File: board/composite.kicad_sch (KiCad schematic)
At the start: 23 parts, among them J10 VGA, J6 COMPOSITE, U17 OBVID, Y1 14.318MHz, Y3 25.175MHz

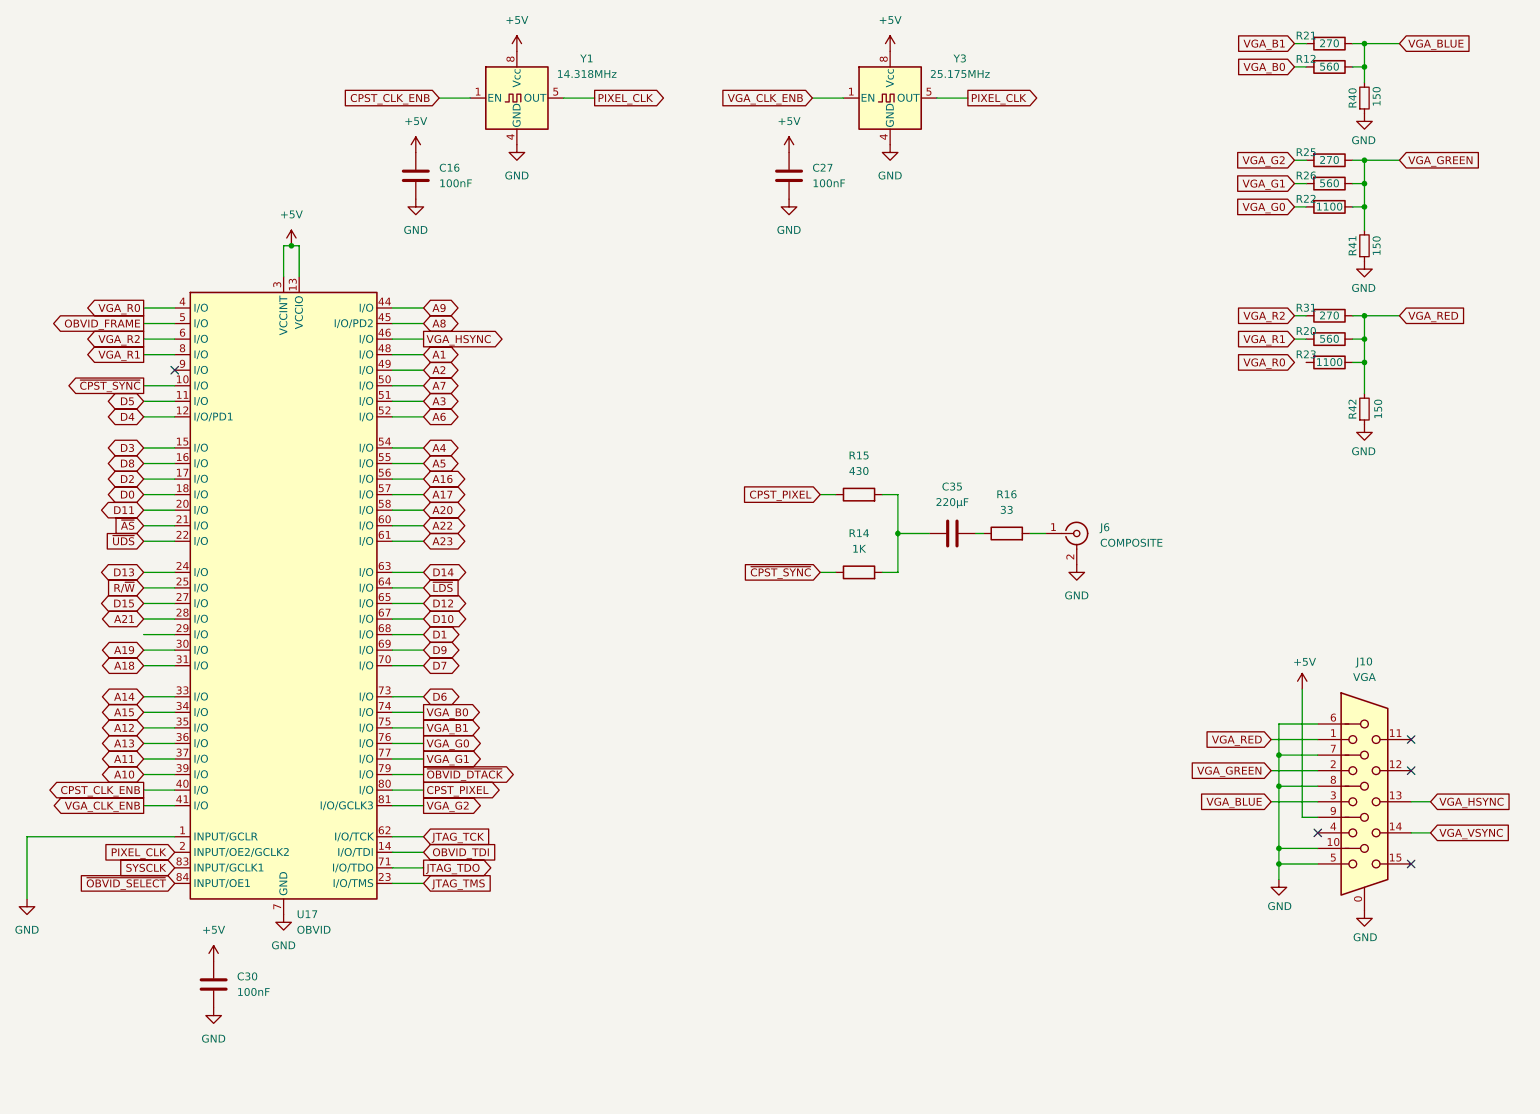
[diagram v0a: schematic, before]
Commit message: CF card, composite, VGA
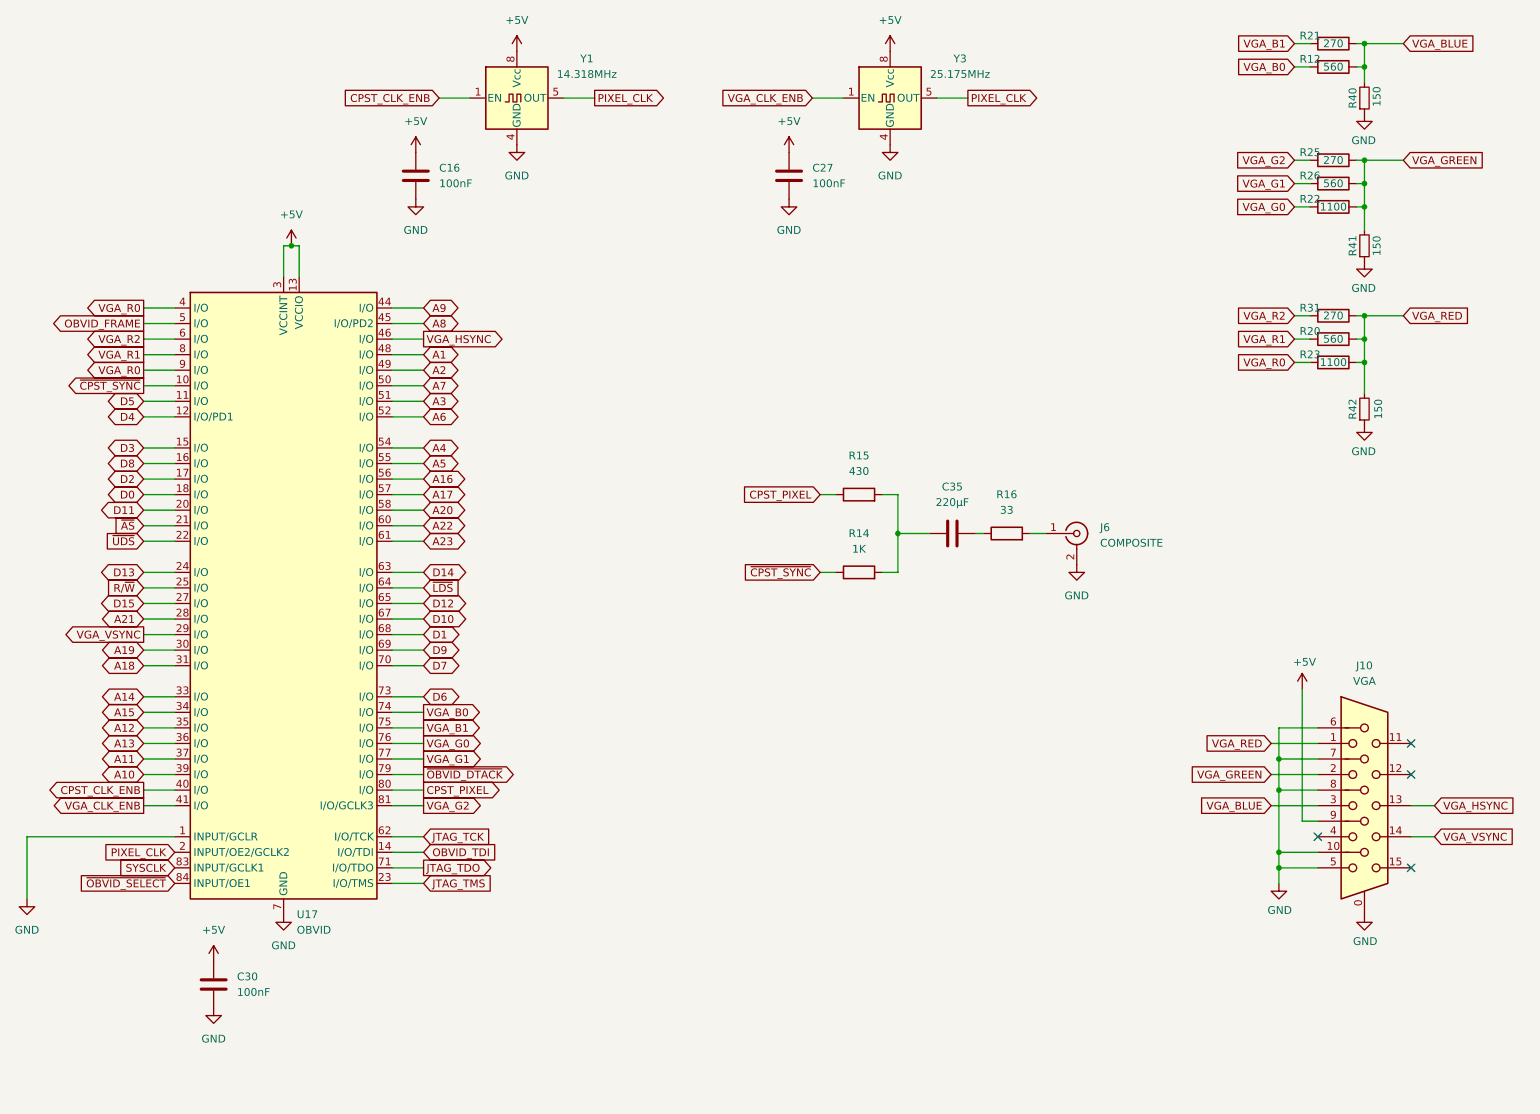
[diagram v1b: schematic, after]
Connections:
- net VGA_R0: now also R23.2, U17.9 (I/O)
- net VGA_VSYNC: now also U17.29 (I/O)
- no-connect marks 5 -> 4
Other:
- moved on the sheet: J10, R12, R20, R21, R22, R23, R25, R26, R31

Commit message: checkpoint
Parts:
- R22, R23: footprint Resistor_SMD:R_0603_1608Metric -> Resistor_THT:R_Axial_DIN0207_L6.3mm_D2.5mm_P10.16mm_Horizontal
- Y3: Digikey https://www.digikey.com/en/products/detail/shenzhen-sctf-electronics/SXOA14-31818A20F30TNN/25795979 -> https://www.digikey.com/en/products/detail/shenzhen-sctf-electronics/SXOA25-175A20F30TNN/25795923?s=N4IgjCBcpgbFoDGUBmBDANgZwKYBoQB7KAbRACYBOAFgAZZKQBdAgBwBcoQBldgJwCWAOwDmIAL4Fq8aCGSR02fEVIUArAHZ6zNp0g9%2BwsZJAMEc1JlwFikMtTBgAHJQ06QHLr0GiJBDRCy8orWKnYgAMwRYGpObiweegY%2BxgSOtObBVsq2ZBHU1OS0GQme%2Bt5GfuBOEZmWSjaqheQalIylSRW%2BJuRq5HUK2Y3h5GDksGDxul6G3QS9tUH1obkUE9TuZcmVPRoySMs5quTUlJMQHTMpVVpuS4MNYWQX0%2BWzqeCOgQcPK6oviSuOzSY2%2BFl%2BR3CMTiERKr22c3AETUG3uIUhz02nXeVRixQG6OGz1OtH6lze1xMYEoLgJQyeIBKPVolH6aPpqwBWy6H1Gagy7Meq16ADpJmoAAQAWQAEgAvLFcACqQgE7AA8igpTg0FgAK58HBVchRJx0oWqKL8yhwwEU4EgAC0YKyFvCsT6zBMjtRP0JDNgESoZO9anNfyh8XE0aAA
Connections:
- net A12 renamed ~{FC2}
- net A14 renamed ~{FC0}
- net A15 renamed ~{FC1}
- net OBVID_FRAME renamed ~{OBVID_IRQ}
- net SYSCLK renamed CPUCLK
- net ~{OBVID_DTACK} renamed OBVID_STALL
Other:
- moved on the sheet: C30, U17

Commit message: Board rev1 PCB complete, already have a spot fix
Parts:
- added J5: JTAG BYPASS, Connector_PinHeader_2.54mm:PinHeader_1x02_P2.54mm_Vertical, symbol Connector:Conn_01x02_Pin
- J10: footprint board:HD15-SN-24 -> board:AMPHENOL_ICD15S13E4GX00LF; symbol Connector:DE15_Socket_HighDensity_MountingHoles -> HD15:ICD15S13E4GX00LF; DigiKey (none) -> https://www.digikey.com/en/products/detail/amphenol-cs-fci/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; MANUFACTURER (none) -> Amphenol; MAXIMUM_PACKAGE_HEIGHT (none) -> 12.96mm; PARTREV (none) -> G; STANDARD (none) -> Manufacturer Recommendations
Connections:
- net +5V: no longer J10.9
- net GND: now also J10.S1 (SHIELD), J10.S2 (SHIELD__1); no longer J10.0, U17.1 (INPUT/GCLR)
- net JTAG_TDO: now also J5.2 (Pin_2)
- net OBVID_TDI: now also J5.1 (Pin_1)
- net VGA_R0: no longer U17.9 (I/O)
- net A10: no longer names the net of U17.39 (I/O)
- net A11: no longer names the net of U17.37 (I/O)
- net A13: no longer names the net of U17.36 (I/O)
- net A16: no longer names the net of U17.56 (I/O)
- net A17: no longer names the net of U17.57 (I/O)
- net A18: no longer names the net of U17.31 (I/O)
- net A19: no longer names the net of U17.30 (I/O)
- net A20: no longer names the net of U17.58 (I/O)
- net A21: no longer names the net of U17.28 (I/O)
- net A22: no longer names the net of U17.60 (I/O)
- net A23: no longer names the net of U17.61 (I/O)
- net A6: no longer names the net of U17.52 (I/O)
- net A7: no longer names the net of U17.50 (I/O)
- net A8: no longer names the net of U17.45 (I/O/PD2)
- net A9: no longer names the net of U17.44 (I/O)
- net ~{FC0} renamed FC0
- net ~{FC1} renamed FC1
- net ~{FC2} renamed FC2
- new net ~{RESET}: U17.1 (INPUT/GCLR)
- no-connect marks 4 -> 21
